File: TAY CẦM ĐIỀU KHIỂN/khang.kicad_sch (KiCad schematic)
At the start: 5 parts, among them U1 ESP32-WROOM-32, U2 NRF24L01_Breakout

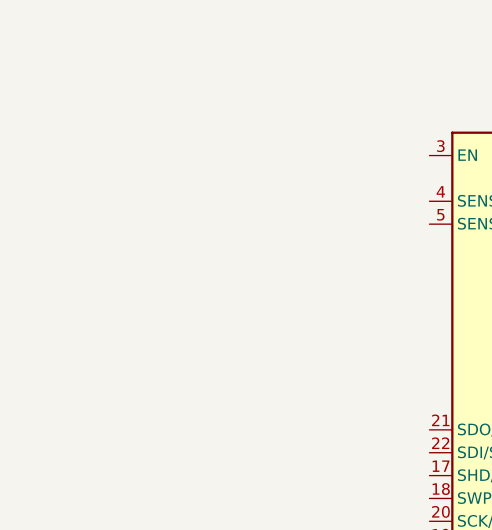
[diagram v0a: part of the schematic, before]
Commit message: ve lai schematic cua tay cam, PCB DNHK da ve on
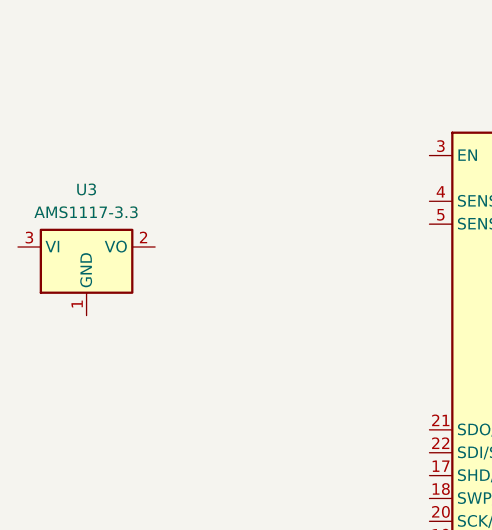
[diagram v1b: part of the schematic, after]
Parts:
- added U3: AMS1117-3.3, Package_TO_SOT_SMD:SOT-223-3_TabPin2, symbol Regulator_Linear:AMS1117-3.3
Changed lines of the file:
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@@
+	)
+	(symbol
+		(lib_id "Regulator_Linear:AMS1117-3.3")
+		(at 114.3 66.04 0)
+		(unit 1)
+		(body_style 1)
+		(exclude_from_sim no)
+		(in_bom yes)
+		(on_board yes)
+		(in_pos_files yes)
+		(dnp no)
+		(fields_autoplaced yes)
+		(property "Reference" "U3"
+			(at 114.3 59.69 0)
+			(show_name no)
+			(do_not_autoplace no)
+			(effects
+				(font
+					(size 1.27 1.27)
+				)
+			)
+		)
+		(property "Value" "AMS1117-3.3"
+			(at 114.3 62.23 0)
+			(show_name no)
+			(do_not_autoplace no)
+			(effects
+				(font
+					(size 1.27 1.27)
+				)
+			)
+		)
+		(property "Footprint" "Package_TO_SOT_SMD:SOT-223-3_TabPin2"
+			(at 114.3 60.96 0)
+			(hide yes)
+			(show_name no)
+			(do_not_autoplace no)
+			(effects
+				(font
+					(size 1.27 1.27)
+				)
+			)
+		)
+		(property "Datasheet" "http://www.advanced-monolithic.com/pdf/ds1117.pdf"
+			(at 116.84 72.39 0)
+			(hide yes)
+			(show_name no)
+			(do_not_autoplace no)
+			(effects
+				(font
+					(size 1.27 1.27)
+				)
+			)
+		)
+		(property "Description" "1A Low Dropout regulator, positive, 3.3V fixed output, SOT-223"
+			(at 114.3 66.04 0)
+			(hide yes)
+			(show_name no)
+			(do_not_autoplace no)
+			(effects
+				(font
+					(size 1.27 1.27)
+				)
+			)
+		)
+		(pin "3"
+		)
+		(pin "2"
+		)
+		(pin "1"
+		)
+		(instances
+			(project "khang"
+				(path "/0218c2fc-33bd-47e8-8d16-439b9ea24079"
+					(reference "U3")
+					(unit 1)
+				)
+			)
+		)
 	)
 	(symbol
